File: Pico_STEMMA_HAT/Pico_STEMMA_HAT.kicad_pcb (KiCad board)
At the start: 2 copper layers, 58 x 63 mm, 38 parts

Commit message: Add STEMMA connector pads to the GND net
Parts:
- D1: value PWRLED -> LED
- renumbered DECOUCAP to C9, RIGHT to J1, LEFT to J2, PCA9548 to TCA9548A1
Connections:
- S1 pad S1: (no net) -> GND
- S1 pad S2: (no net) -> GND
- S2 pad S1: (no net) -> GND
- S2 pad S2: (no net) -> GND
- S3 pad S1: (no net) -> GND
- S3 pad S2: (no net) -> GND
- S4 pad S1: (no net) -> GND
- S4 pad S2: (no net) -> GND
- S5 pad S1: (no net) -> GND
- S5 pad S2: (no net) -> GND
- S6 pad S1: (no net) -> GND
- S6 pad S2: (no net) -> GND
- S7 pad S1: (no net) -> GND
- S8 pad S1: (no net) -> GND
- S8 pad S2: (no net) -> GND
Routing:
- net +3V3: track 277.1 -> 288.7 mm
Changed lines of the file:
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@@
 	(net 50 "/SCL7")
 	(net 51 "/SDA7")
-	(net 52 "unconnected-(U2-A1-Pad2)")
-	(net 53 "unconnected-(U2-A0-Pad1)")
-	(net 54 "unconnected-(U2-#RESET-Pad3)")
-	(net 55 "unconnected-(U2-A2-Pad21)")
+	(net 52 "unconnected-(TCA9548A1-A1-Pad2)")
+	(net 53 "unconnected-(TCA9548A1-A0-Pad1)")
+	(net 54 "unconnected-(TCA9548A1-#RESET-Pad3)")
+	(net 55 "unconnected-(TCA9548A1-A2-Pad21)")
 	(footprint "Connector_PinSocket_2.54mm:PinSocket_1x20_P2.54mm_Vertical"
 		(layer "F.Cu")
@@
 		(descr "Through hole straight socket strip, 1x20, 2.54mm pitch, single row (from Kicad 4.0.7), script generated")
 		(tags "Through hole socket strip THT 1x20 2.54mm single row")
-		(property "Reference" "RIGHT"
+		(property "Reference" "J1"
 			(at 0 -2.77 0)
 			(layer "F.SilkS")
@@
 			(size 1.2 1.8)
 			(layers "F.Cu" "F.Paste" "F.Mask")
+			(net 1 "GND")
 			(solder_mask_margin 0.102)
 		)
@@
 			(size 1.2 1.8)
 			(layers "F.Cu" "F.Paste" "F.Mask")
+			(net 1 "GND")
 			(solder_mask_margin 0.102)
 		)
@@
 			(size 1.2 1.8)
 			(layers "F.Cu" "F.Paste" "F.Mask")
+			(net 1 "GND")
 			(solder_mask_margin 0.102)
 		)
@@
 			(size 1.2 1.8)
 			(layers "F.Cu" "F.Paste" "F.Mask")
+			(net 1 "GND")
 			(solder_mask_margin 0.102)
 		)
@@
 			(size 1.2 1.8)
 			(layers "F.Cu" "F.Paste" "F.Mask")
+			(net 1 "GND")
 			(solder_mask_margin 0.102)
 		)
@@
 			(size 1.2 1.8)
 			(layers "F.Cu" "F.Paste" "F.Mask")
+			(net 1 "GND")
 			(solder_mask_margin 0.102)
 		)
@@
 			(size 1.2 1.8)
 			(layers "F.Cu" "F.Paste" "F.Mask")
+			(net 1 "GND")
 			(solder_mask_margin 0.102)
 		)
@@
 			(size 1.2 1.8)
 			(layers "F.Cu" "F.Paste" "F.Mask")
+			(net 1 "GND")
 			(solder_mask_margin 0.102)
 		)
@@
 		(descr "Capacitor SMD 0603 (1608 Metric), square (rectangular) end terminal, IPC_7351 nominal, (Body size source: IPC-SM-782 page 76, https://www.pcb-3d.com/wordpress/wp-content/uploads/ipc-sm-782a_amendment_1_and_2.pdf), generated with kicad-footprint-generator")
 		(tags "capacitor")
-		(property "Reference" "DECOUCAP"
+		(property "Reference" "C9"
 			(at 2.25 0 0)
 			(layer "F.SilkS")
@@
 			(size 1.2 1.8)
 			(layers "F.Cu" "F.Paste" "F.Mask")
+			(net 1 "GND")
 			(solder_mask_margin 0.102)
 		)
@@
 			(size 1.2 1.8)
 			(layers "F.Cu" "F.Paste" "F.Mask")
+			(net 1 "GND")
 			(solder_mask_margin 0.102)
 		)
@@
 			(size 1.2 1.8)
 			(layers "F.Cu" "F.Paste" "F.Mask")
+			(net 1 "GND")
 			(solder_mask_margin 0.102)
 		)
@@
 		(descr "Through hole straight socket strip, 1x20, 2.54mm pitch, single row (from Kicad 4.0.7), script generated")
 		(tags "Through hole socket strip THT 1x20 2.54mm single row")
-		(property "Reference" "LEFT"
+		(property "Reference" "J2"
 			(at 0 -2.77 0)
 			(layer "F.SilkS")
@@
 			(size 1.2 1.8)
 			(layers "F.Cu" "F.Paste" "F.Mask")
+			(net 1 "GND")
 			(solder_mask_margin 0.102)
 		)
@@
 			(size 1.2 1.8)
 			(layers "F.Cu" "F.Paste" "F.Mask")
+			(net 1 "GND")
 			(solder_mask_margin 0.102)
 		)
@@
 			(size 1.2 1.8)
 			(layers "F.Cu" "F.Paste" "F.Mask")
+			(net 1 "GND")
 			(solder_mask_margin 0.102)
 		)
@@
 			(size 1.2 1.8)
 			(layers "F.Cu" "F.Paste" "F.Mask")
+			(net 1 "GND")
 			(solder_mask_margin 0.102)
 		)
@@
 			)
 		)
-		(property "Value" "PWRLED"
+		(property "Value" "LED"
 			(at 1.75 2.75 90)
 			(layer "F.Fab")
@@
 		(at 150 99.75)
 		(tags "TCA9548APWR ")
-		(property "Reference" "PCA9548"
+		(property "Reference" "TCA9548A1"
 			(at -0.25 0 -90)
 			(unlocked yes)
@@
 			(size 1.4732 0.3556)
 			(layers "F.Cu" "F.Paste" "F.Mask")
-			(net 53 "unconnected-(U2-A0-Pad1)")
+			(net 53 "unconnected-(TCA9548A1-A0-Pad1)")
 			(pinfunction "A0")
 			(pintype "bidirectional+no_connect")
@@
 			(size 1.4732 0.3556)
 			(layers "F.Cu" "F.Paste" "F.Mask")
-			(net 52 "unconnected-(U2-A1-Pad2)")
+			(net 52 "unconnected-(TCA9548A1-A1-Pad2)")
 			(pinfunction "A1")
 			(pintype "bidirectional+no_connect")
@@
 			(size 1.4732 0.3556)
 			(layers "F.Cu" "F.Paste" "F.Mask")
-			(net 54 "unconnected-(U2-#RESET-Pad3)")
+			(net 54 "unconnected-(TCA9548A1-#RESET-Pad3)")
 			(pinfunction "#RESET")
 			(pintype "bidirectional+no_connect")
@@
 			(size 1.4732 0.3556)
 			(layers "F.Cu" "F.Paste" "F.Mask")
-			(net 55 "unconnected-(U2-A2-Pad21)")
+			(net 55 "unconnected-(TCA9548A1-A2-Pad21)")
 			(pinfunction "A2")
 			(pintype "bidirectional+no_connect")
@@
 	)
 	(segment
+		(start 135.25 80.575)
+		(end 133.675 79)
+		(width 0.15)
+		(layer "F.Cu")
+		(net 2)
+	)
+	(segment
+		(start 133.675 79)
+		(end 125 79)
+		(width 0.15)
+		(layer "F.Cu")
+		(net 2)
+	)
+	(segment
 		(start 175.75 120)
 		(end 175.75 126.25)
@@
 	)
 	(segment
+		(start 125 79)
+		(end 124.5 78.5)
+		(width 0.15)
+		(layer "F.Cu")
+		(net 2)
+	)
+	(segment
 		(start 124.5 80.75)
 		(end 124.5 80)
@@
 	)
 	(segment
-		(start 124.5 80)
+		(start 124.5 78.5)
 		(end 124.5 77.75)
 		(width 0.6)
@@
 		(width 0.6)
 		(layer "F.Cu")
+		(net 2)
+	)
+	(segment
+		(start 124.5 80)
+		(end 124.5 78.5)
+		(width 0.6)
+		(layer "F.Cu")

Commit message: Add 3D models for STEMMA connectors and TCA9548A
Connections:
- S1 pad S1: GND -> (no net)
- S1 pad S2: GND -> (no net)
- S2 pad S1: GND -> (no net)
- S2 pad S2: GND -> (no net)
- S3 pad S1: GND -> (no net)
- S3 pad S2: GND -> (no net)
- S4 pad S1: GND -> (no net)
- S4 pad S2: GND -> (no net)
- S5 pad S1: GND -> (no net)
- S5 pad S2: GND -> (no net)
- S6 pad S1: GND -> (no net)
- S6 pad S2: GND -> (no net)
- S7 pad S1: GND -> (no net)
- S8 pad S1: GND -> (no net)
- S8 pad S2: GND -> (no net)
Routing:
- net /SCL5: track 21.8 -> 24.0 mm
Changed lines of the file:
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@@
 		(at 123.75 105 -90)
 		(property "Reference" "S3"
-			(at -0.25 0 -90)
+			(at -0.25 0 90)
 			(layer "F.SilkS")
 			(effects
@@
 			(size 1.2 1.8)
 			(layers "F.Cu" "F.Paste" "F.Mask")
-			(net 1 "GND")
 			(solder_mask_margin 0.102)
 		)
@@
 			(size 1.2 1.8)
 			(layers "F.Cu" "F.Paste" "F.Mask")
-			(net 1 "GND")
 			(solder_mask_margin 0.102)
 		)
+		(model "C:/Users/boccs/OneDrive/Desktop/FoldersFiles/REIMAGINED_3D_FILES_BLENDER/PRT-14417.step"
+			(offset
+				(xyz 0 2 -0.3)
+			)
+			(scale
+				(xyz 1 1 1)
+			)
+			(rotate
+				(xyz -90 0 0)
+			)
+		)
 	)
 	(footprint "Resistor_SMD:R_0603_1608Metric"
@@
 			(size 1.2 1.8)
 			(layers "F.Cu" "F.Paste" "F.Mask")
-			(net 1 "GND")
 			(solder_mask_margin 0.102)
 		)
@@
 			(size 1.2 1.8)
 			(layers "F.Cu" "F.Paste" "F.Mask")
-			(net 1 "GND")
 			(solder_mask_margin 0.102)
 		)
+		(model "C:/Users/boccs/OneDrive/Desktop/FoldersFiles/REIMAGINED_3D_FILES_BLENDER/PRT-14417.step"
+			(offset
+				(xyz 0 2 -0.3)
+			)
+			(scale
+				(xyz 1 1 1)
+			)
+			(rotate
+				(xyz -90 0 0)
+			)
+		)
 	)
 	(footprint "Resistor_SMD:R_0603_1608Metric"
@@
 			(size 1.2 1.8)
 			(layers "F.Cu" "F.Paste" "F.Mask")
-			(net 1 "GND")
 			(solder_mask_margin 0.102)
 		)
@@
 			(size 1.2 1.8)
 			(layers "F.Cu" "F.Paste" "F.Mask")
-			(net 1 "GND")
 			(solder_mask_margin 0.102)
 		)
+		(model "C:/Users/boccs/OneDrive/Desktop/FoldersFiles/REIMAGINED_3D_FILES_BLENDER/PRT-14417.step"
+			(offset
+				(xyz 0 2 -0.3)
+			)
+			(scale
+				(xyz 1 1 1)
+			)
+			(rotate
+				(xyz -90 0 0)
+			)
+		)
 	)
 	(footprint "Resistor_SMD:R_0603_1608Metric"
@@
 			(size 1.2 1.8)
 			(layers "F.Cu" "F.Paste" "F.Mask")
-			(net 1 "GND")
 			(solder_mask_margin 0.102)
 		)
@@
 			(size 1.2 1.8)
 			(layers "F.Cu" "F.Paste" "F.Mask")
-			(net 1 "GND")
 			(solder_mask_margin 0.102)
 		)
+		(model "C:/Users/boccs/OneDrive/Desktop/FoldersFiles/REIMAGINED_3D_FILES_BLENDER/PRT-14417.step"
+			(offset
+				(xyz 0 2 -0.3)
+			)
+			(scale
+				(xyz 1 1 1)
+			)
+			(rotate
+				(xyz -90 0 0)
+			)
+		)
 	)
 	(footprint "Capacitor_SMD:C_0603_1608Metric"
@@
 			(size 1.2 1.8)
 			(layers "F.Cu" "F.Paste" "F.Mask")
-			(net 1 "GND")
 			(solder_mask_margin 0.102)
 		)
@@
 			(solder_mask_margin 0.102)
 		)
+		(model "C:/Users/boccs/OneDrive/Desktop/FoldersFiles/REIMAGINED_3D_FILES_BLENDER/PRT-14417.step"
+			(offset
+				(xyz 0 2 -0.3)
+			)
+			(scale
+				(xyz 1 1 1)
+			)
+			(rotate
+				(xyz -90 0 0)
+			)
+		)
 	)
 	(footprint "Pico_Footprints:STEMMAQWIIC_Footprint"
@@
 			(size 1.2 1.8)
 			(layers "F.Cu" "F.Paste" "F.Mask")
-			(net 1 "GND")
 			(solder_mask_margin 0.102)
 		)
@@
 			(size 1.2 1.8)
 			(layers "F.Cu" "F.Paste" "F.Mask")
-			(net 1 "GND")
 			(solder_mask_margin 0.102)
 		)
+		(model "C:/Users/boccs/OneDrive/Desktop/FoldersFiles/REIMAGINED_3D_FILES_BLENDER/PRT-14417.step"
+			(offset
+				(xyz 0 2 -0.3)
+			)
+			(scale
+				(xyz 1 1 1)
+			)
+			(rotate
+				(xyz -90 0 0)
+			)
+		)
 	)
 	(footprint "Capacitor_SMD:C_0603_1608Metric"
@@
 			(size 1.2 1.8)
 			(layers "F.Cu" "F.Paste" "F.Mask")
-			(net 1 "GND")
 			(solder_mask_margin 0.102)
 		)
@@
 			(size 1.2 1.8)
 			(layers "F.Cu" "F.Paste" "F.Mask")
-			(net 1 "GND")
 			(solder_mask_margin 0.102)
 		)
+		(model "C:/Users/boccs/OneDrive/Desktop/FoldersFiles/REIMAGINED_3D_FILES_BLENDER/PRT-14417.step"
+			(offset
+				(xyz 0 2 -0.3)
+			)
+			(scale
+				(xyz 1 1 1)
+			)
+			(rotate
+				(xyz -90 0 0)
+			)
+		)
 	)
 	(footprint "Resistor_SMD:R_0603_1608Metric"
@@
 			(size 1.2 1.8)
 			(layers "F.Cu" "F.Paste" "F.Mask")
-			(net 1 "GND")
 			(solder_mask_margin 0.102)
 		)
@@
 			(size 1.2 1.8)
 			(layers "F.Cu" "F.Paste" "F.Mask")
-			(net 1 "GND")
 			(solder_mask_margin 0.102)
 		)
+		(model "C:/Users/boccs/OneDrive/Desktop/FoldersFiles/REIMAGINED_3D_FILES_BLENDER/PRT-14417.step"
+			(offset
+				(xyz 0 2 -0.3)
+			)
+			(scale
+				(xyz 1 1 1)
+			)
+			(rotate
+				(xyz -90 0 0)
+			)
+		)
 	)
 	(footprint "LED_SMD:LED_0603_1608Metric"
@@
 		(fp_text user "*"
 			(at -3.175 -5.0736 0)
-			(unlocked yes)
 			(layer "F.SilkS")
 			(effects
@@
 		(fp_text user "*"
 			(at -1.8669 -3.8735 0)
+			(unlocked yes)
 			(layer "F.Fab")
 			(effects
@@
 			(pintype "bidirectional")
 		)
+		(model "C:/Users/boccs/OneDrive/Desktop/FoldersFiles/REIMAGINED_3D_FILES_BLENDER/PW0024A.stp"
+			(offset
+				(xyz 0 0 0)
+			)
+			(scale
+				(xyz 1 1 1)
+			)
+			(rotate
+				(xyz 0 0 0)
+			)
+		)
 	)
 	(gr_line
@@
 		(width 0.15)
 		(layer "F.Cu")
+		(net 46)
+	)
+	(segment
+		(start 174.05 103.5)
+		(end 171.825 103.5)
+		(width 0.15)
+		(layer "F.Cu")

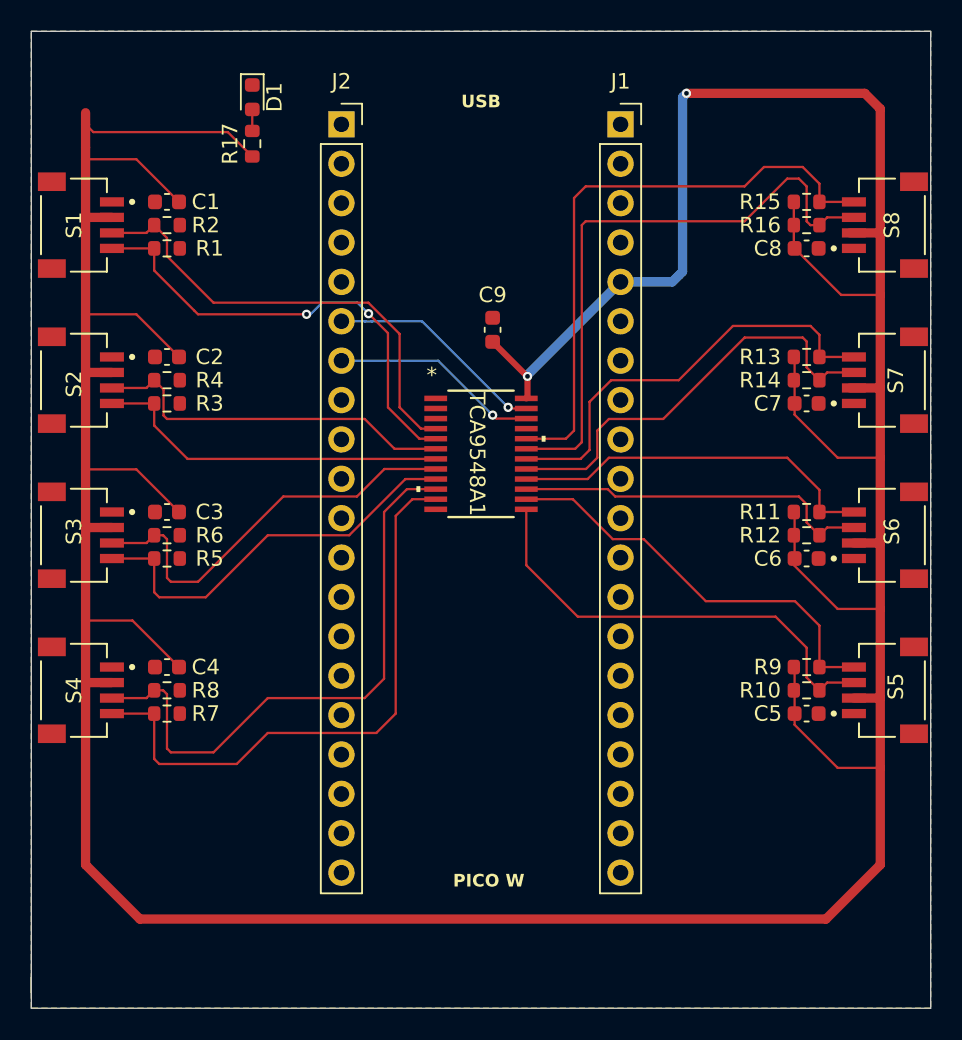
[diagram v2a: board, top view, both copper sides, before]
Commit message: Fix errors from the DRC
The design rules are based around the JLCPCB manufacturer
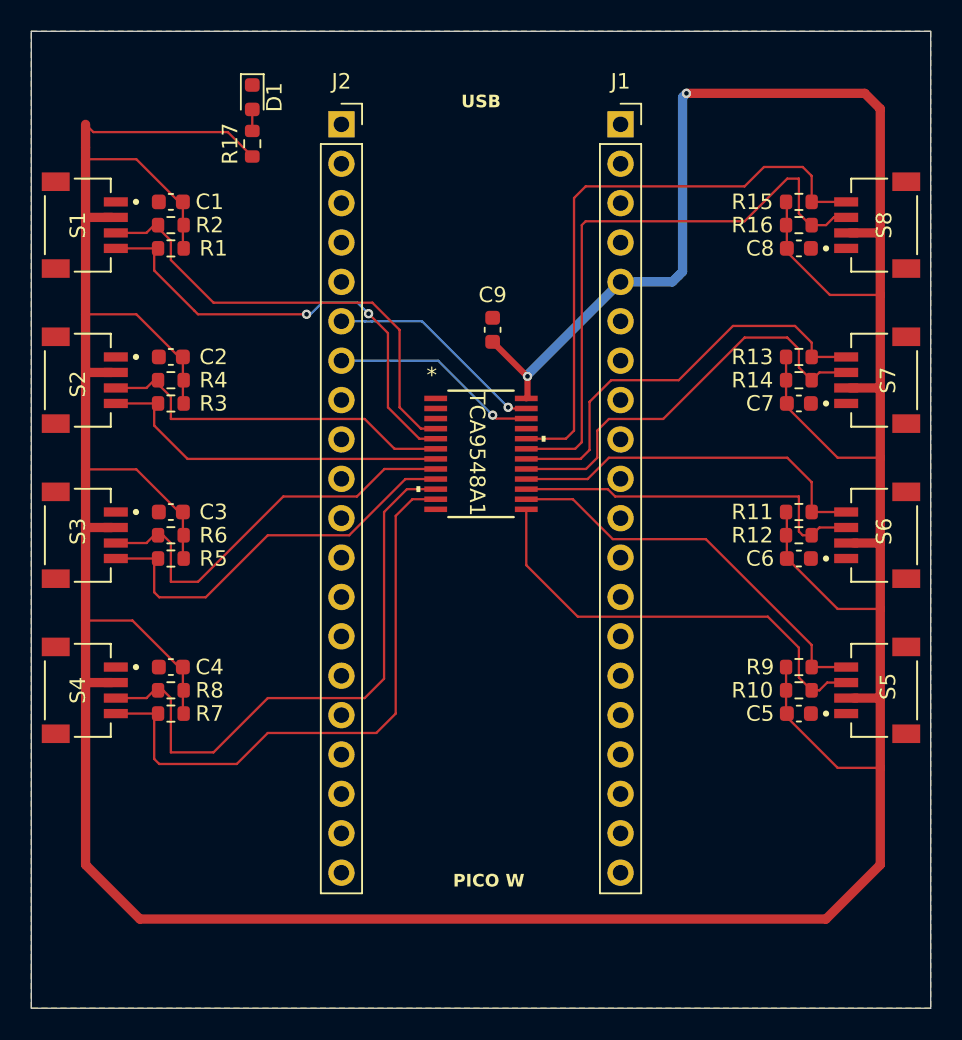
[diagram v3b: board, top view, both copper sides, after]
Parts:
- moved C5 0.50 mm to (170.5, 116.5)
- moved C6 0.50 mm to (170.5, 106.5)
- moved C7 0.50 mm to (170.5, 96.5)
- moved C8 0.50 mm to (170.5, 86.5)
- moved R10 0.50 mm to (170.5, 115.0)
- moved R11 0.50 mm to (170.5, 103.5)
- moved R12 0.50 mm to (170.5, 105.0)
- moved R13 0.50 mm to (170.5, 93.5)
- moved R14 0.50 mm to (170.5, 95.0)
- moved R15 0.50 mm to (170.5, 83.5)
- moved R16 0.50 mm to (170.5, 85.0)
- moved R9 0.50 mm to (170.5, 113.5)
- moved S5 0.50 mm to (176.0, 115.0)
- moved S6 0.50 mm to (176.0, 105.0)
- moved S7 0.50 mm to (176.0, 95.0)
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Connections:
- S1 pad S1: (no net) -> GND
- S1 pad S2: (no net) -> GND
- S2 pad S1: (no net) -> GND
- S2 pad S2: (no net) -> GND
- S3 pad S1: (no net) -> GND
- S3 pad S2: (no net) -> GND
- S4 pad S1: (no net) -> GND
- S4 pad S2: (no net) -> GND
- S5 pad S1: (no net) -> GND
- S5 pad S2: (no net) -> GND
- S6 pad S1: (no net) -> GND
- S6 pad S2: (no net) -> GND
- S7 pad S1: (no net) -> GND
- S7 pad S2: (no net) -> GND
- S8 pad S1: (no net) -> GND
- S8 pad S2: (no net) -> GND
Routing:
- net +3V3: track 288.7 -> 301.2 mm
- net /SDA6: track 28.0 -> 27.2 mm
- net /SCL6: track 28.2 -> 27.4 mm
- net /SCL4: track 27.2 -> 26.4 mm
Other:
- outline, holes or cut-outs redrawn

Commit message: Rearranged traces
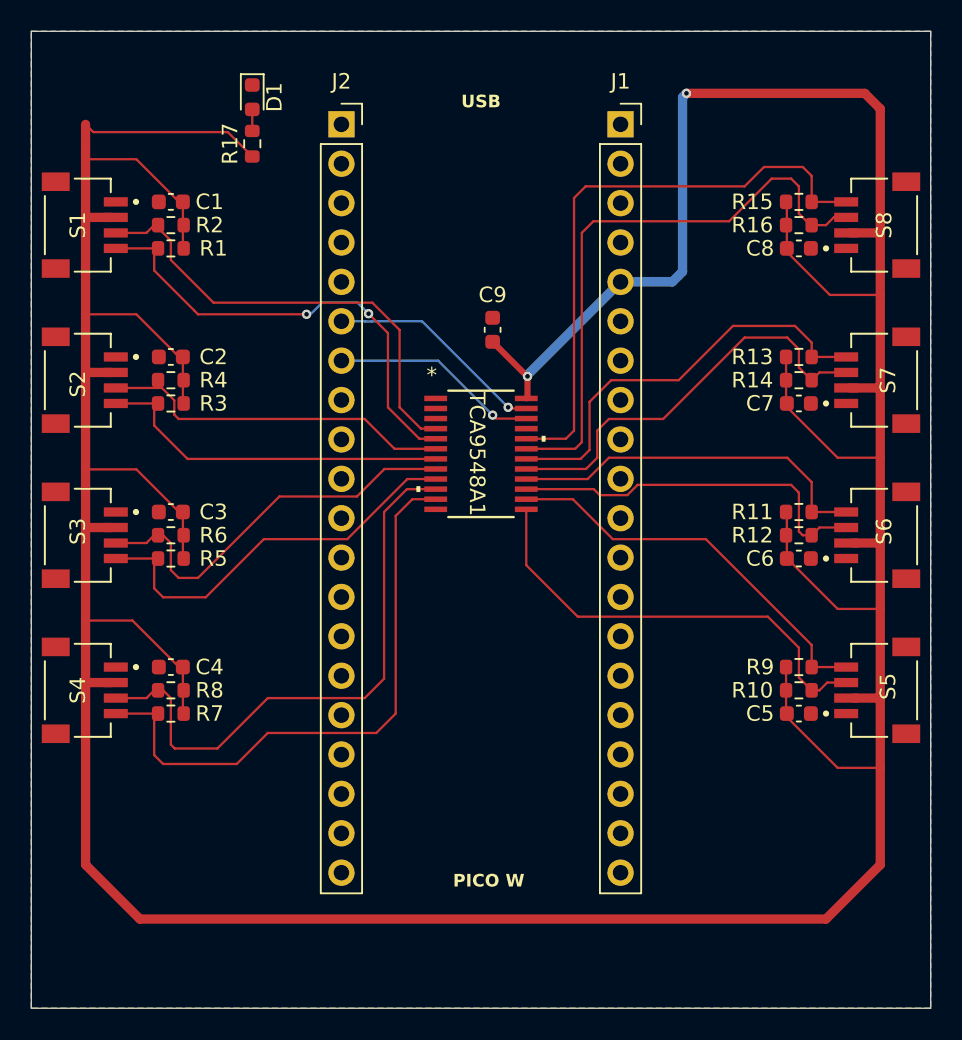
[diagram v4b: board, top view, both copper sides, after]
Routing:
- net /SDA1: track 23.8 -> 23.0 mm
- net /SDA5: track 23.4 -> 24.1 mm
- net /SDA2: track 27.1 -> 26.5 mm
- net /SDA7: track 39.3 -> 38.7 mm
- net /SDA3: track 38.1 -> 37.6 mm
